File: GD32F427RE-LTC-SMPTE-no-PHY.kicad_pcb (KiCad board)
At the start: 2 copper layers, 66.6 x 69.3 mm, 64 parts, among them J1 BOOT0, J10 GPS, J11 GPIO 5V, J2 USART0, J3 GPIO, J4 I2C, J5 I2C LCD/KEYS, J6 External PHY, J7 MIDI, J8 SPI, J9 LTC, SW1 BOOT0, SW2 RESET, U1 GT-USB-7010ASV, U2 AMS1117-3.3, U3 W25Q128JVS, U4 74LVC2G125, U5 74LVC2G125, U6 GD32F427RET6, X1 25Mhz, X2 32.768kHz

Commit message: Fix PA3-PA5 pin labels
Correct the PA3, PA4, and PA5 labels in the schematic and PCB silkscreen so the header pin names match the intended mapping. The 3D board render is updated to reflect the corrected labeling.
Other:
- board text added: "PA3"
- board text removed: "PA6"
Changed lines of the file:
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@@
 		)
 	)
-	(gr_text "PA4"
+	(gr_text "PA3"
 		(at 68.2 79.8 90)
 		(layer "F.SilkS")
@@
 		)
 	)
-	(gr_text "PA5"
+	(gr_text "PA4"
 		(at 70.65 79.8 90)
 		(layer "F.SilkS")
@@
 		)
 	)
-	(gr_text "PA6"
+	(gr_text "PA5"
 		(at 73.2 79.8 90)
 		(layer "F.SilkS")

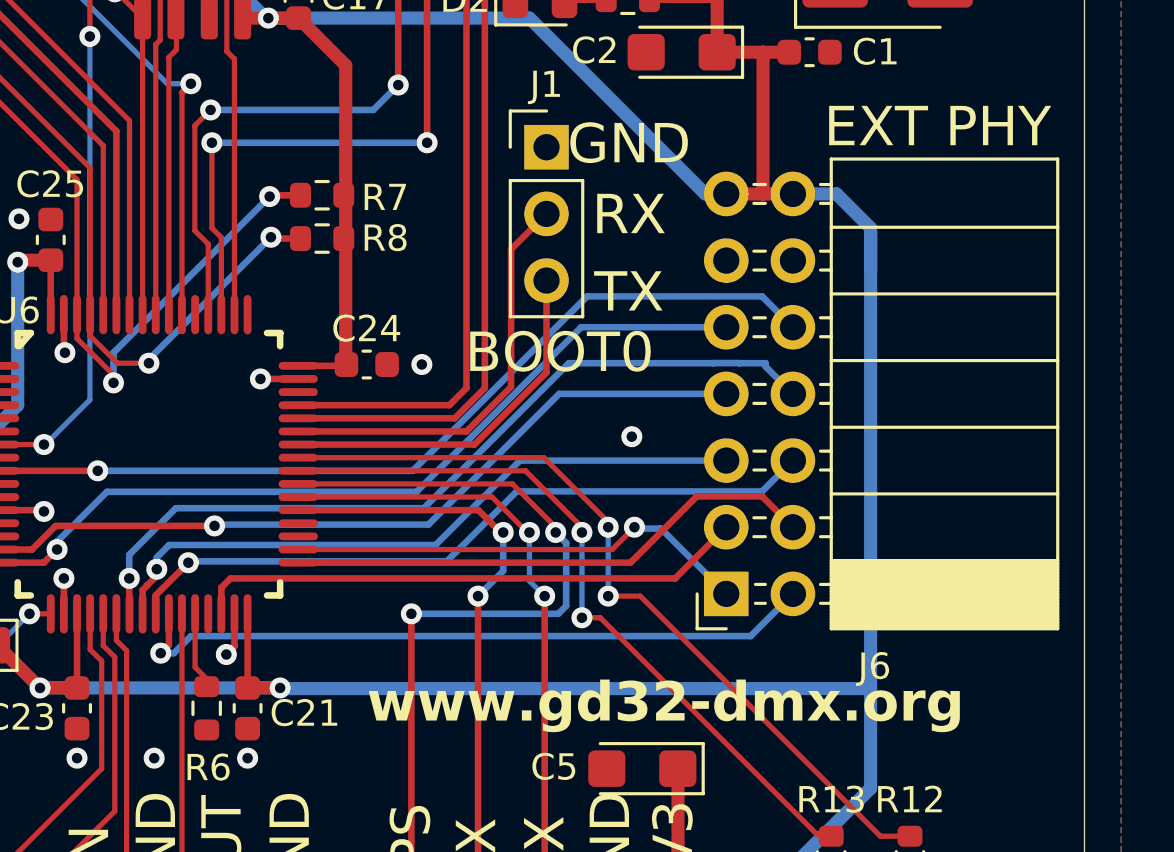
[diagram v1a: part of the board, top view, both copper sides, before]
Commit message: Fix PA3-PA5 net mapping and shift J6 connector
Corrects the net assignments on the MCU pins (PA3, PA4, PA5) and the corresponding J6 header pads, which were off by one (PA4/PA5/PA6). Tracks and vias are renamed to match.

Moves J6 (2x07 socket) 0.9 mm in X (102 -> 102.9) and reroutes the +3V3, MDC, RMII_CRS_DV, RMII_RXD1, RMII_TXD0, RMII_TXD1 and PHY_INT traces to follow it. Adds three GND stitching vias and refreshes the GND zone fills.
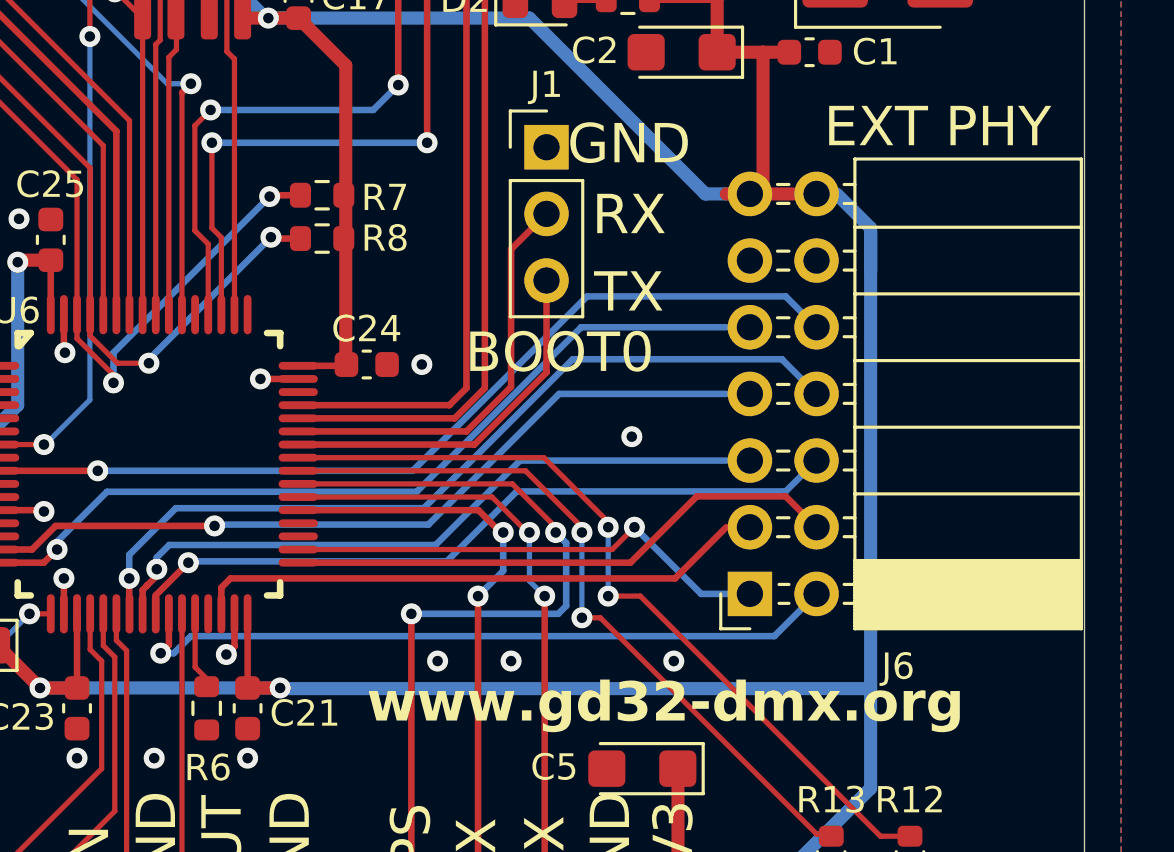
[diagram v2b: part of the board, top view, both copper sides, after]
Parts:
- moved J6 0.90 mm to (102.9, 69.9)
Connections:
- J3 pad 2: /PA4 -> /PA3
- J3 pad 3: /PA5 -> /PA4
- J3 pad 4: /PA6 -> /PA5
- U6 pad 17: /PA4 -> /PA3
- U6 pad 20: /PA5 -> /PA4
- U6 pad 21: /PA6 -> /PA5
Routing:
- net /PA3: track 0.00 -> 16.8 mm, vias 0 -> 1
- net /PA6: track 15.5 -> 0.00 mm
- net /PA5: track 16.5 -> 15.5 mm
- net /RMII_CRS_DV: track 31.1 -> 32.1 mm
- net /RMII_RXD1: track 27.1 -> 28.0 mm
- net /MDC: track 33.5 -> 34.4 mm
- net /RMII_TXD0: track 20.4 -> 21.3 mm
- net /~{PHY_INT}: track 26.7 -> 27.6 mm
- net +3V3: track 239.0 -> 239.8 mm
- net /RMII_TXD1: track 17.7 -> 18.5 mm
- net /PA4: track 16.8 -> 16.5 mm, vias 1 -> 0
- net GND: vias 20 -> 23
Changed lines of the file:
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@@
 			(size 1.5 0.3)
 			(layers "F.Cu" "F.Mask" "F.Paste")
-			(net "/PA4")
+			(net "/PA3")
 			(pinfunction "PA3_17")
 			(pintype "bidirectional")
@@
 			(size 1.5 0.3)
 			(layers "F.Cu" "F.Mask" "F.Paste")
-			(net "/PA5")
+			(net "/PA4")
 			(pinfunction "PA4_20")
 			(pintype "bidirectional")
@@
 			(size 1.5 0.3)
 			(layers "F.Cu" "F.Mask" "F.Paste")
-			(net "/PA6")
+			(net "/PA5")
 			(pinfunction "PA5_21")
 			(pintype "bidirectional")
@@
 	(footprint "Connector_PinSocket_2.54mm:PinSocket_2x07_P2.54mm_Horizontal"
 		(layer "F.Cu")
-		(at 102 69.94 180)
+		(at 102.9 69.94 180)
 		(descr "Through hole angled socket strip, 2x07, 2.54mm pitch, 8.51mm socket length, double rows (from Kicad 4.0.7), script generated")
 		(tags "Through hole angled socket strip THT 2x07 2.54mm double row")
@@
 			(layers "*.Cu" "*.Mask")
 			(remove_unused_layers no)
-			(net "/PA4")
+			(net "/PA3")
 			(pinfunction "Pin_2_2")
 			(pintype "passive")
@@
 			(layers "*.Cu" "*.Mask")
 			(remove_unused_layers no)
-			(net "/PA5")
+			(net "/PA4")
 			(pinfunction "Pin_3_3")
 			(pintype "passive")
@@
 			(layers "*.Cu" "*.Mask")
 			(remove_unused_layers no)
-			(net "/PA6")
+			(net "/PA5")
 			(pinfunction "Pin_4_4")
 			(pintype "passive")
@@
 	)
 	(via
+		(at 91 72.5)
+		(size 0.8)
+		(drill 0.4)
+		(layers "F.Cu" "B.Cu")
+		(free yes)
+		(net "GND")
+	)
+	(via
 		(at 70.05 68.6)
 		(size 0.8)
@@
 	)
 	(via
+		(at 100 72.5)
+		(size 0.8)
+		(drill 0.4)
+		(layers "F.Cu" "B.Cu")
+		(free yes)
+		(net "GND")
+	)
+	(via
 		(at 90.4 61.2)
 		(size 0.8)
@@
 	)
 	(via
+		(at 93.8 72.5)
+		(size 0.8)
+		(drill 0.4)
+		(layers "F.Cu" "B.Cu")
+		(free yes)
+		(net "GND")
+	)
+	(via
 		(at 76.8 60.75)
 		(size 0.8)
@@
 	)
 	(segment
-		(start 100.16 83.7)
-		(end 101.15 83.7)
-		(width 0.5)
+		(start 105.44 54.7)
+		(end 102.9 54.7)
+		(width 0.25)
 		(layer "B.Cu")
 		(net "+3V3")
 	)
 	(segment
-		(start 104.54 54.7)
-		(end 106.2 54.7)
+		(start 100.16 83.7)
+		(end 101.15 83.7)
 		(width 0.5)
 		(layer "B.Cu")
@@
 	)
 	(segment
-		(start 104.54 59.78)
-		(end 103.365 58.605)
+		(start 90.05 65.25)
+		(end 78.05 65.25)
 		(width 0.25)
 		(layer "B.Cu")
@@
 	)
 	(segment
-		(start 103.365 58.605)
-		(end 96.695 58.605)
+		(start 105.44 59.78)
+		(end 104.265 58.605)
 		(width 0.25)
 		(layer "B.Cu")
@@
 	)
 	(segment
-		(start 90.05 65.25)
-		(end 78.05 65.25)
+		(start 104.265 58.605)
+		(end 96.695 58.605)
 		(width 0.25)
 		(layer "B.Cu")
@@
 	)
 	(segment
-		(start 76.26 70.7)
-		(end 75.45 70.7)
-		(width 0.2)
-		(layer "F.Cu")
-		(net "/PA4")
-	)
-	(via
-		(at 75.45 70.7)
-		(size 0.8)
-		(drill 0.4)
-		(layers "F.Cu" "B.Cu")
-		(net "/PA4")
-	)
-	(segment
-		(start 68.14 78.01)
-		(end 68.14 83.7)
-		(width 0.2)
-		(layer "B.Cu")
-		(net "/PA4")
-	)
-	(segment
-		(start 75.45 70.7)
-		(end 68.14 78.01)
-		(width 0.2)
-		(layer "B.Cu")
-		(net "/PA4")
-	)
-	(segment
 		(start 77.76 70.7)
 		(end 77.76 72.06)
 		(width 0.2)
 		(layer "F.Cu")
-		(net "/PA5")
+		(net "/PA4")
 	)
 	(segment
@@
 		(width 0.2)
 		(layer "F.Cu")
-		(net "/PA5")
+		(net "/PA4")
 	)
 	(segment
@@
 		(width 0.2)
 		(layer "F.Cu")
-		(net "/PA5")
+		(net "/PA4")
 	)
 	(segment
@@
 		(width 0.2)
 		(layer "F.Cu")
-		(net "/PA5")
+		(net "/PA4")
 	)
 	(segment
@@
 		(width 0.2)
 		(layer "F.Cu")
-		(net "/PA5")
+		(net "/PA4")
 	)
 	(segment
@@
 		(width 0.2)
 		(layer "F.Cu")
-		(net "/PA5")
+		(net "/PA4")
 	)
 	(segment
@@
 		(width 0.2)
 		(layer "F.Cu")
-		(net "/PA6")
+		(net "/PA5")
 	)
 	(segment
@@
 		(width 0.2)
 		(layer "F.Cu")
-		(net "/PA6")
+		(net "/PA5")
 	)
 	(segment
@@
 		(width 0.2)
 		(layer "F.Cu")
-		(net "/PA6")
+		(net "/PA5")
 	)
 	(segment
@@
 		(width 0.2)
 		(layer "F.Cu")
-		(net "/PA6")
+		(net "/PA5")
 	)
 	(segment
@@
 	)
 	(segment
-		(start 81.025 66.675)
-		(end 79.25 68.45)
-		(width 0.25)
-		(layer "B.Cu")
-		(net "/RMII_CRS_DV")
-	)
-	(segment
 		(start 79.25 68.45)
 		(end 79.25 69.35)
@@
 	)
 	(segment
-		(start 101.513299 61.145)
-		(end 101.508299 61.15)
-		(width 0.25)
-		(layer "B.Cu")
-		(net "/RMII_CRS_DV")
-	)
-	(segment
-		(start 101.508299 61.15)
-		(end 96 61.15)
-		(width 0.25)
-		(layer "B.Cu")
-		(net "/RMII_CRS_DV")
-	)
-	(segment
-		(start 104.54 62.32)
-		(end 103.5 61.28)
-		(width 0.25)
-		(layer "B.Cu")
-		(net "/RMII_CRS_DV")
-	)
-	(segment
-		(start 102.486701 61.145)
-		(end 101.513299 61.145)
+		(start 81.025 66.675)
+		(end 79.25 68.45)
 		(width 0.25)
 		(layer "B.Cu")
@@
 	)
 	(segment
-		(start 96 61.15)
+		(start 96.15 61)
 		(end 90.475 66.675)
 		(width 0.25)
@@
 	)
 	(segment
-		(start 103.5 61.15)
-		(end 102.491701 61.15)
-		(width 0.25)
-		(layer "B.Cu")
-		(net "/RMII_CRS_DV")
-	)
-	(segment
-		(start 102.491701 61.15)
-		(end 102.486701 61.145)
+		(start 104.12 61)
+		(end 96.15 61)
 		(width 0.25)
 		(layer "B.Cu")
@@
 	)
 	(segment
-		(start 103.5 61.28)
-		(end 103.5 61.15)
+		(start 105.44 62.32)
+		(end 104.12 61)
 		(width 0.25)
 		(layer "B.Cu")
@@
 	)
 	(segment
-		(start 81.553934 68.7)
-		(end 81.501967 68.751967)
+		(start 105.44 64.86)
+		(end 104.265 66.035)
 		(width 0.25)
 		(layer "B.Cu")
@@
 	)
 	(segment
-		(start 91.35 68.7)
-		(end 81.553934 68.7)
+		(start 94.015 66.035)
+		(end 91.35 68.7)
 		(width 0.25)
 		(layer "B.Cu")
@@
 	)
 	(segment
-		(start 94.015 66.035)
-		(end 91.35 68.7)
+		(start 81.553934 68.7)
+		(end 81.501967 68.751967)
 		(width 0.25)
 		(layer "B.Cu")
@@
 	)
 	(segment
-		(start 104.54 64.86)
-		(end 103.365 66.035)
+		(start 104.265 66.035)
+		(end 94.015 66.035)
 		(width 0.25)
 		(layer "B.Cu")
@@
 	)
 	(segment
-		(start 103.365 66.035)
-		(end 94.015 66.035)
+		(start 91.35 68.7)
+		(end 81.553934 68.7)
 		(width 0.25)
 		(layer "B.Cu")
@@
 	)
 	(segment
-		(start 81.6 71.55)
-		(end 102.93 71.55)
+		(start 103.83 71.55)
+		(end 81.6 71.55)
 		(width 0.25)
 		(layer "B.Cu")
@@
 	)
 	(segment
-		(start 80.45 72.2)
-		(end 80.95 72.2)
+		(start 80.95 72.2)
+		(end 80.45 72.2)
 		(width 0.25)
 		(layer "B.Cu")
@@
 	)
 	(segment
-		(start 80.95 72.2)
-		(end 81.6 71.55)
+		(start 105.44 69.94)
+		(end 103.83 71.55)
 		(width 0.25)
 		(layer "B.Cu")
@@
 	)
 	(segment
-		(start 102.93 71.55)
-		(end 104.54 69.94)
+		(start 81.6 71.55)
+		(end 80.95 72.2)
 		(width 0.25)
 		(layer "B.Cu")
@@
 	)
 	(segment
-		(start 98.35 68.75)
-		(end 85.69 68.75)
+		(start 104.265 66.225)
+		(end 100.875 66.225)
 		(width 0.25)
 		(layer "F.Cu")
@@
 	)
 	(segment
-		(start 104.54 67.4)
-		(end 103.365 66.225)
+		(start 105.44 67.4)
+		(end 104.265 66.225)
 		(width 0.25)
 		(layer "F.Cu")
@@
 	)
 	(segment
-		(start 103.365 66.225)
-		(end 100.875 66.225)
+		(start 100.875 66.225)
+		(end 98.35 68.75)
 		(width 0.25)
 		(layer "F.Cu")
@@
 	)
 	(segment
-		(start 100.875 66.225)
-		(end 98.35 68.75)
+		(start 98.35 68.75)
+		(end 85.69 68.75)
 		(width 0.25)
 		(layer "F.Cu")
@@
 	)
 	(segment
-		(start 99.51 67.45)
-		(end 98.45 67.45)
+		(start 102.9 69.94)
+		(end 101.04 69.94)
 		(width 0.25)
 		(layer "B.Cu")
@@
 	)
 	(segment
-		(start 102 69.94)
-		(end 99.51 67.45)
+		(start 101.04 69.94)
+		(end 98.5 67.4)
 		(width 0.25)
 		(layer "B.Cu")
@@
 		(net "/SPI_MOSI")
 	)
+	(segment
+		(start 76.26 70.7)
+		(end 75.45 70.7)
+		(width 0.2)
+		(layer "F.Cu")
+		(net "/PA3")
+	)
+	(via
+		(at 75.45 70.7)
+		(size 0.8)
+		(drill 0.4)
+		(layers "F.Cu" "B.Cu")
+		(net "/PA3")
+	)
+	(segment
+		(start 68.14 78.01)
+		(end 68.14 83.7)
+		(width 0.2)
+		(layer "B.Cu")
+		(net "/PA3")
+	)
+	(segment
+		(start 75.45 70.7)
+		(end 68.14 78.01)
+		(width 0.2)
+		(layer "B.Cu")
+		(net "/PA3")
+	)
 	(zone
